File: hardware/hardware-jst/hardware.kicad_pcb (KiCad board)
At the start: 2 copper layers, 123.4 x 109.1 mm, 81 parts, among them J2 Barrel_Jack, M1 Stepper_Motor_unipolar_5pin, M10 Stepper_Motor_unipolar_5pin, M11 Stepper_Motor_unipolar_5pin, M12 Stepper_Motor_unipolar_5pin, M13 Stepper_Motor_unipolar_5pin, M14 Stepper_Motor_unipolar_5pin, M2 Stepper_Motor_unipolar_5pin, M3 Stepper_Motor_unipolar_5pin, M4 Stepper_Motor_unipolar_5pin, M5 Stepper_Motor_unipolar_5pin, M6 Stepper_Motor_unipolar_5pin, M7 Stepper_Motor_unipolar_5pin, M8 Stepper_Motor_unipolar_5pin, M9 Stepper_Motor_unipolar_5pin, SW1 SW_Push_SPDT, SW10 SW_Push_SPDT, SW11 SW_Push_SPDT, SW12 SW_Push_SPDT, SW13 SW_Push_SPDT, SW14 SW_Push_SPDT, SW15 SW_Push_SPDT, SW16 SW_Push_SPDT, SW2 SW_Push_SPDT, SW3 SW_Push_SPDT, SW4 SW_Push_SPDT, SW5 SW_Push_SPDT, SW6 SW_Push_SPDT, SW7 SW_Push_SPDT, SW8 SW_Push_SPDT, SW9 SW_Push_SPDT, U1 WeMos_D1_mini, U10 ULN2003A, U11 ULN2003A, U12 ULN2003A, U13 ULN2003A, U14 ULN2003A, U15 ULN2003A, U16 ULN2003A, U17 ULN2003A, U2 CD4051B, U3 CD4051B, U4 ULN2003A, U5 ULN2003A, U6 ULN2003A, U7 ULN2003A, U8 ULN2003A, U9 ULN2003A

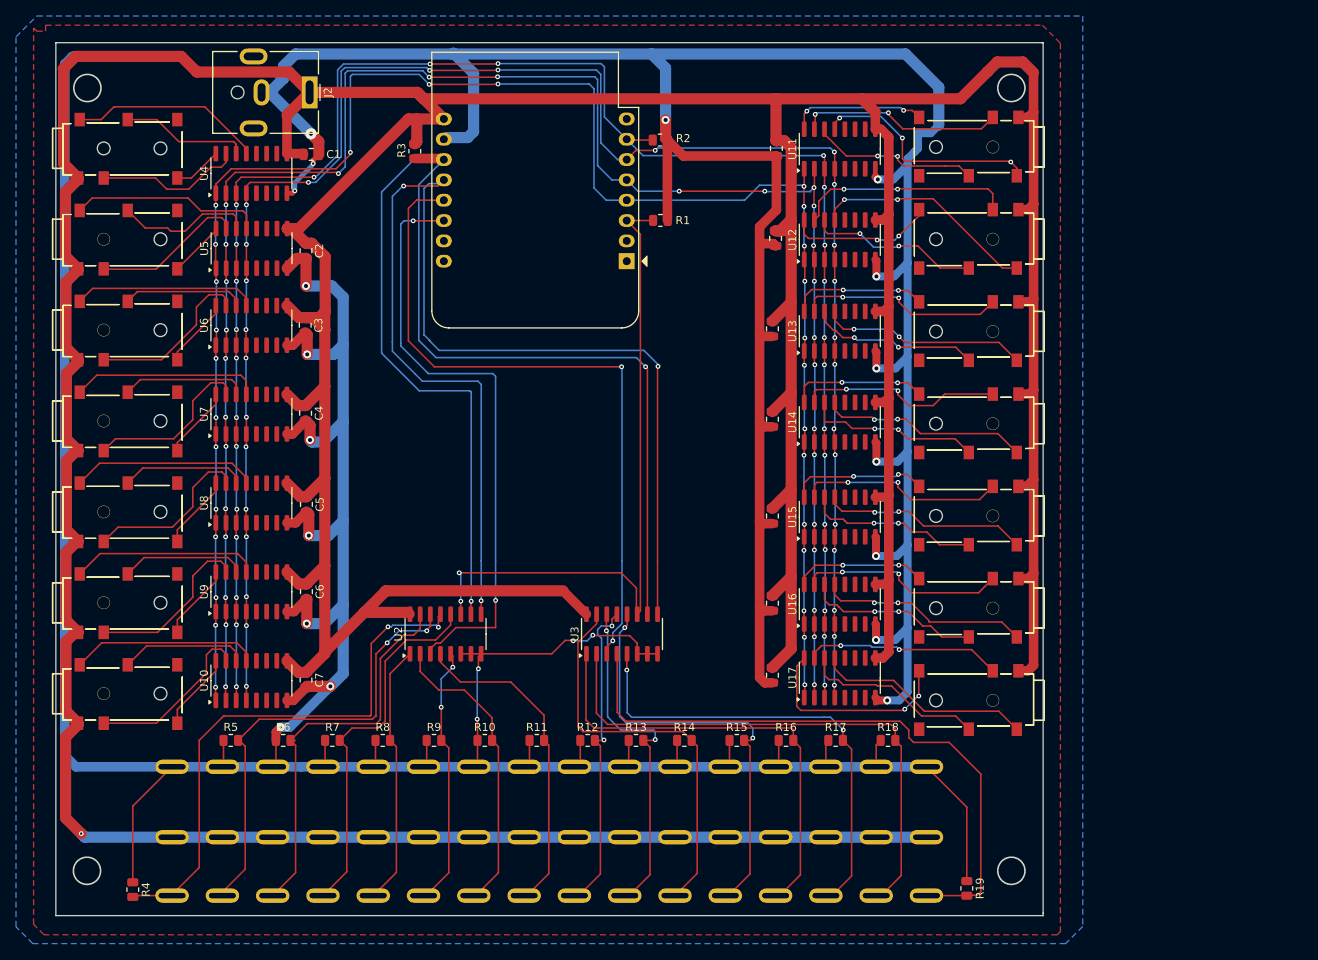
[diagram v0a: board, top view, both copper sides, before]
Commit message: partial jst conversion of pcb
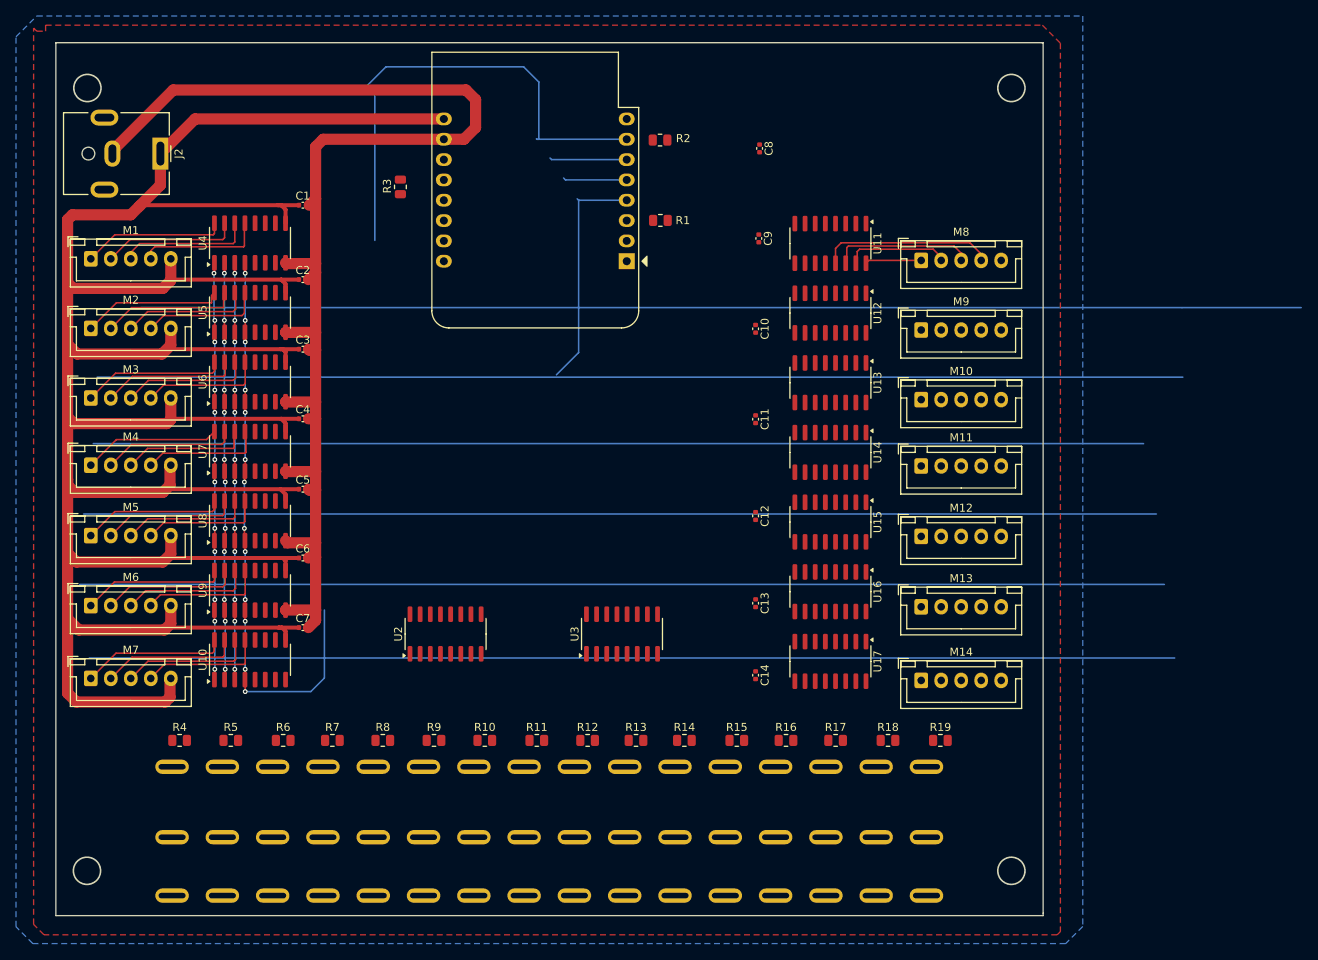
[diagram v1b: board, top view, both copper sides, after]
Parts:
- C1, C10, C11, C12, C13, C14, C2, C3, C4, C5, C6, C7, C8, C9: footprint Capacitor_SMD:C_0805_2012Metric -> Capacitor_SMD:C_0402_1005Metric
- M1, M10, M11, M12, M13, M14, M2, M3, M4, M5, M6, M7, M8, M9: footprint Connector_Audio:HOOYA-PJ-3505A_C19190915-Jack_3.5mm_PJ31060-I_Horizontal -> Connector_JST:JST_XH_B5B-XH-A_1x05_P2.50mm_Vertical
- moved J2 20.2 mm to (171.0, 57.4)
- moved R4 19.5 mm to (173.4, 130.7), turned to 0 degrees
- moved R19 18.8 mm to (268.5, 130.7), turned to 0 degrees
- moved M1 15.0 mm to (162.3, 70.5), turned to 0 degrees
- moved M8 15.0 mm to (266.1, 70.7), turned to 0 degrees
- moved M2 12.6 mm to (162.3, 79.2), turned to 0 degrees
- moved M9 12.3 mm to (266.1, 79.4), turned to 0 degrees
- moved U11 11.9 mm to (254.8, 68.6), turned to -90 degrees
- moved M3 10.4 mm to (162.3, 87.9), turned to 0 degrees
- moved M10 9.70 mm to (266.1, 88.1), turned to 0 degrees
- moved U12 9.23 mm to (254.8, 77.3), turned to -90 degrees
- moved U4 8.70 mm to (182.2, 68.5)
- moved M4 8.26 mm to (162.3, 96.3), turned to 0 degrees
- moved U5 8.01 mm to (182.2, 77.2)
- moved U6 7.07 mm to (182.2, 85.9)
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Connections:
- M1 pad 1: RED -> BLUE1
- M1 pad 2: ORANGE1 -> PINK1
- M1 pad 3: PINK1 -> YELLOW1
- M1 pad 4: YELLOW1 -> ORANGE1
- M1 pad 5: BLUE1 -> RED
- M10 pad 1: RED -> BLUE10
- M10 pad 2: ORANGE10 -> PINK10
- M10 pad 3: PINK10 -> YELLOW10
- M10 pad 4: YELLOW10 -> ORANGE10
- M10 pad 5: BLUE10 -> RED
- M11 pad 1: RED -> BLUE11
- M11 pad 2: ORANGE11 -> PINK11
- M11 pad 3: PINK11 -> YELLOW11
- M11 pad 4: YELLOW11 -> ORANGE11
- M11 pad 5: BLUE11 -> RED
- M12 pad 1: RED -> BLUE12
- M12 pad 2: ORANGE12 -> PINK12
- M12 pad 3: PINK12 -> YELLOW12
- M12 pad 4: YELLOW12 -> ORANGE12
- M12 pad 5: BLUE12 -> RED
- M13 pad 1: RED -> BLUE13
- M13 pad 2: ORANGE13 -> PINK13
- M13 pad 3: PINK13 -> YELLOW13
- M13 pad 4: YELLOW13 -> ORANGE13
- M13 pad 5: BLUE13 -> RED
- M14 pad 1: RED -> BLUE14
- M14 pad 2: ORANGE14 -> PINK14
- M14 pad 3: PINK14 -> YELLOW14
- M14 pad 4: YELLOW14 -> ORANGE14
- M14 pad 5: BLUE14 -> RED
- M2 pad 1: RED -> BLUE2
- M2 pad 2: ORANGE2 -> PINK2
- M2 pad 3: PINK2 -> YELLOW2
- M2 pad 4: YELLOW2 -> ORANGE2
- M2 pad 5: BLUE2 -> RED
- M3 pad 1: RED -> BLUE3
- M3 pad 2: ORANGE3 -> PINK3
- M3 pad 3: PINK3 -> YELLOW3
- M3 pad 4: YELLOW3 -> ORANGE3
- M3 pad 5: BLUE3 -> RED
- M4 pad 1: RED -> BLUE4
- M4 pad 2: ORANGE4 -> PINK4
- M4 pad 3: PINK4 -> YELLOW4
- M4 pad 4: YELLOW4 -> ORANGE4
- M4 pad 5: BLUE4 -> RED
- M5 pad 1: RED -> BLUE5
- M5 pad 2: ORANGE5 -> PINK5
- M5 pad 3: PINK5 -> YELLOW5
- M5 pad 4: YELLOW5 -> ORANGE5
- M5 pad 5: BLUE5 -> RED
- M6 pad 1: RED -> BLUE6
- M6 pad 2: ORANGE6 -> PINK6
- M6 pad 3: PINK6 -> YELLOW6
- M6 pad 4: YELLOW6 -> ORANGE6
- M6 pad 5: BLUE6 -> RED
- M7 pad 1: RED -> BLUE7
- M7 pad 2: ORANGE7 -> PINK7
- M7 pad 3: PINK7 -> YELLOW7
- M7 pad 4: YELLOW7 -> ORANGE7
- M7 pad 5: BLUE7 -> RED
- M8 pad 1: RED -> BLUE8
- M8 pad 2: ORANGE8 -> PINK8
- M8 pad 3: PINK8 -> YELLOW8
- M8 pad 4: YELLOW8 -> ORANGE8
- M8 pad 5: BLUE8 -> RED
- M9 pad 1: RED -> BLUE9
- M9 pad 2: ORANGE9 -> PINK9
- M9 pad 3: PINK9 -> YELLOW9
- M9 pad 4: YELLOW9 -> ORANGE9
- M9 pad 5: BLUE9 -> RED
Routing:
- net GND: track 822.2 -> 163.8 mm, vias 22 -> 0
- net RED: track 778.0 -> 360.9 mm, vias 1 -> 0
- net IN2: track 230.3 -> 60.3 mm, vias 30 -> 12
- net B: track 158.9 -> 0.00 mm, vias 2 -> 0
- net C: track 151.6 -> 0.00 mm, vias 3 -> 0
- net IN1: track 232.0 -> 81.6 mm, vias 28 -> 12
- net IN4: track 229.4 -> 82.6 mm, vias 29 -> 13
- net IN3: track 230.5 -> 113.6 mm, vias 28 -> 12
- net MUX2COM: track 86.2 -> 0.00 mm, vias 2 -> 0
- net A: track 84.9 -> 0.00 mm, vias 2 -> 0
- net SW16: track 78.2 -> 0.00 mm
- net MUX1COM: track 75.5 -> 0.00 mm, vias 2 -> 0
- net SW1: track 68.7 -> 0.00 mm, vias 2 -> 0
- net SW15: track 68.4 -> 0.00 mm
- net SW14: track 58.2 -> 0.00 mm, vias 2 -> 0
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
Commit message: half way done
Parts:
- moved C8 11.4 mm to (248.4, 67.8), turned to 90 degrees
- moved C9 6.94 mm to (248.1, 74.5)
- moved C10 4.87 mm to (245.4, 84.1)
- moved C11 4.87 mm to (245.4, 95.4)
- moved C13 4.87 mm to (245.4, 118.4)
- moved C12 4.87 mm to (245.4, 107.5)
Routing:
- net RED: track 360.9 -> 813.3 mm
- net GND: track 163.8 -> 225.9 mm
- net IN1: track 81.6 -> 103.6 mm, vias 12 -> 15
- net ORANGE9: track 0.00 -> 21.4 mm
- net YELLOW9: track 0.00 -> 16.7 mm
- net PINK9: track 0.00 -> 12.5 mm
- net BLUE9: track 0.00 -> 7.05 mm

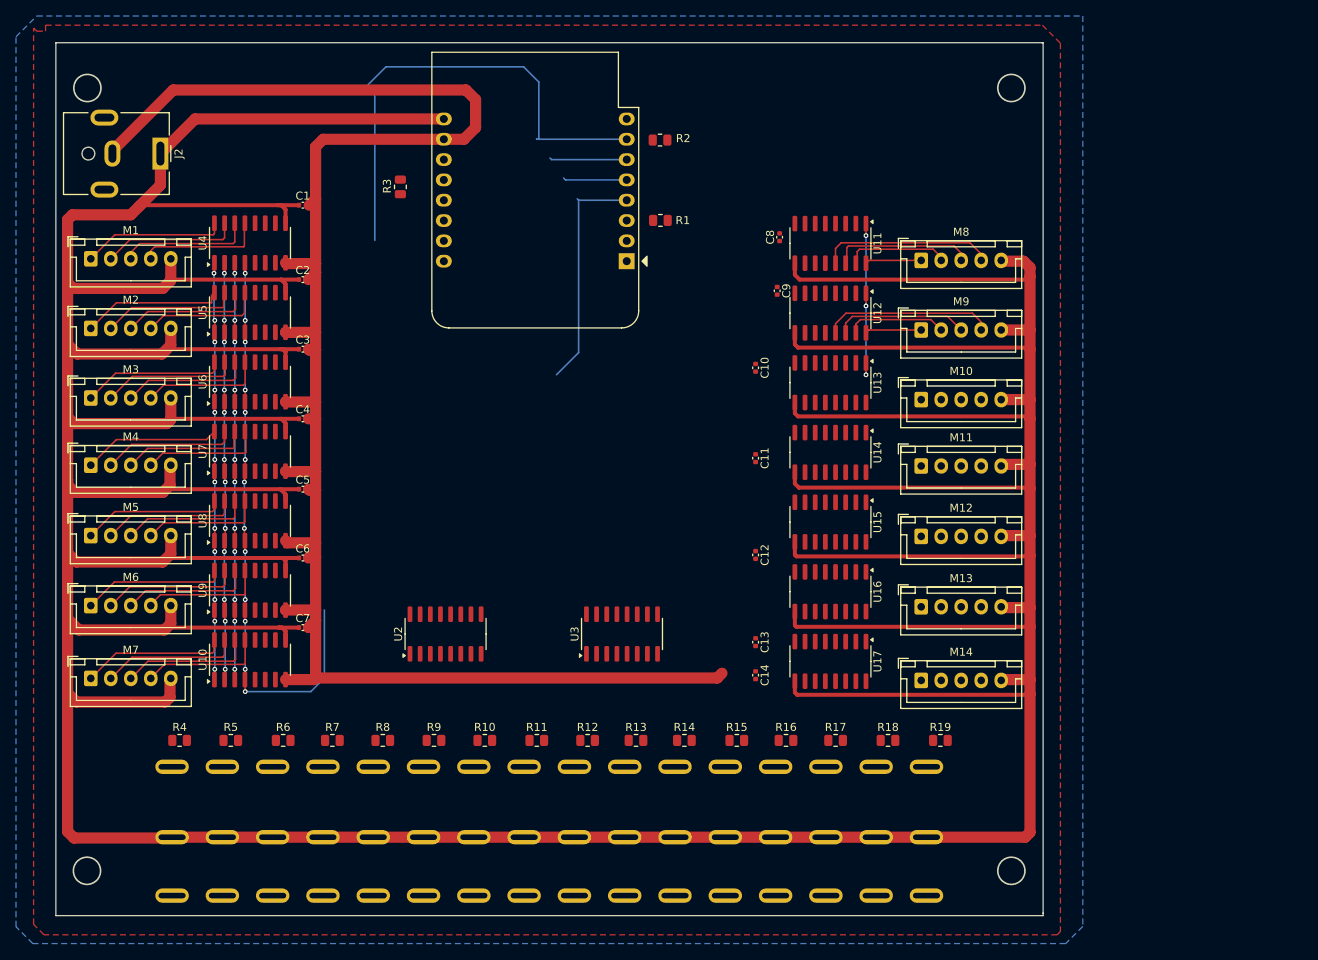
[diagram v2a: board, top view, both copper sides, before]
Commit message: finalised JST switch version of the pcb
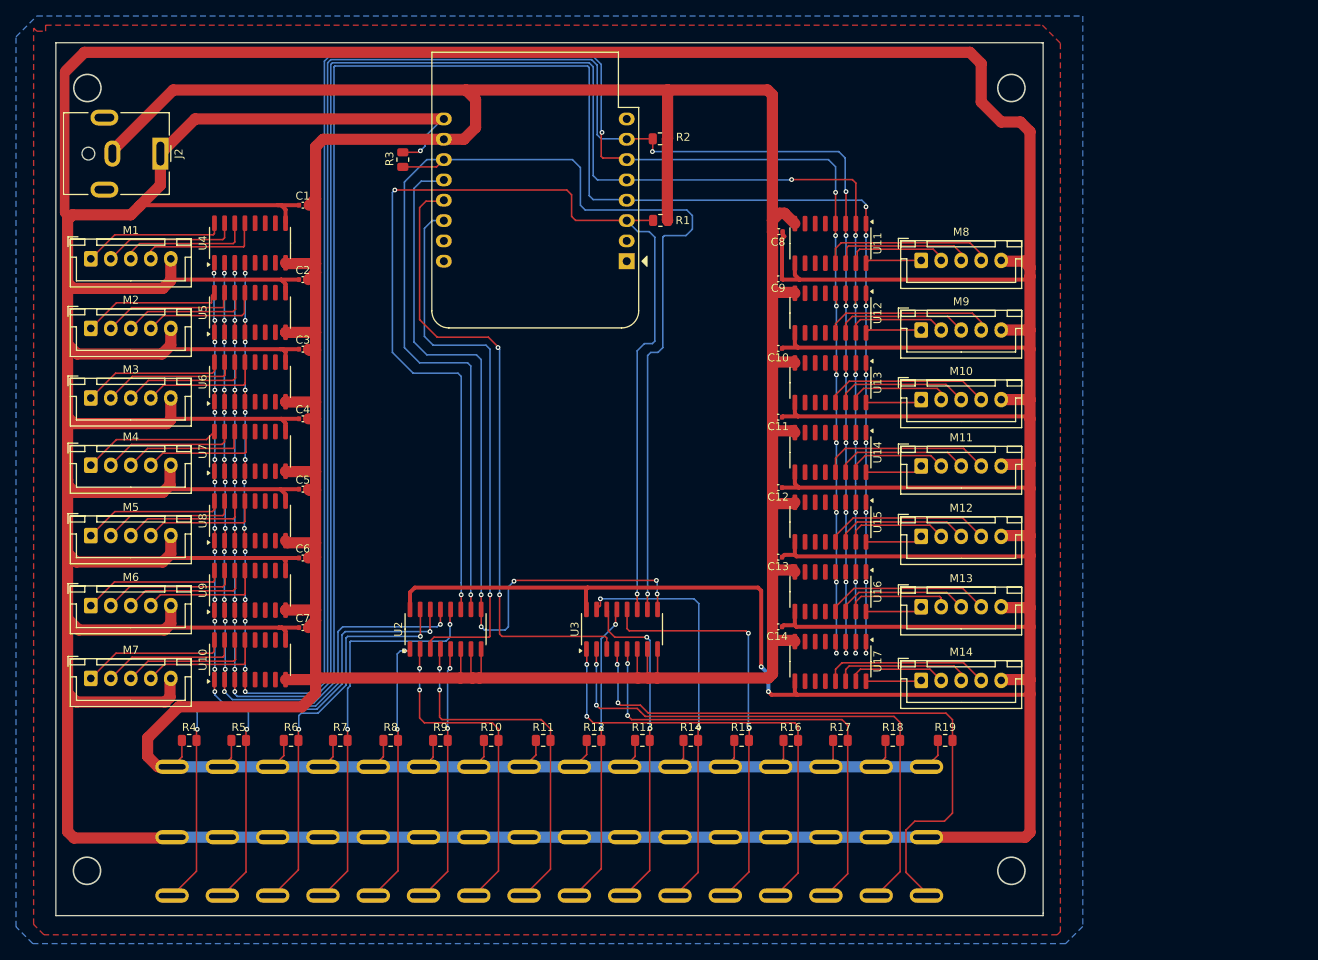
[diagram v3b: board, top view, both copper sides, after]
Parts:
- moved C13 11.0 mm to (248.2, 107.8), turned to 180 degrees
- moved C12 8.88 mm to (248.2, 99.1), turned to 180 degrees
- moved C14 6.67 mm to (248.2, 116.5), turned to 180 degrees
- moved C11 5.85 mm to (248.2, 90.3), turned to 180 degrees
- moved C10 3.72 mm to (248.2, 81.7), turned to 180 degrees
- moved R3 3.43 mm to (201.3, 58.1)
- moved C9 1.50 mm to (248.2, 73.0), turned to 180 degrees
- moved R4 1.20 mm to (174.6, 130.7)
- moved R6 0.99 mm to (187.3, 130.7)
- moved R7 0.99 mm to (193.5, 130.7)
- moved R5 0.99 mm to (180.8, 130.7)
- moved R8 0.99 mm to (199.8, 130.7)
- moved R13 0.80 mm to (231.2, 130.7)
- moved R14 0.80 mm to (237.3, 130.7)
- moved R9 0.80 mm to (206.0, 130.7)
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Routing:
- net GND: track 225.9 -> 588.9 mm
- net RED: track 813.3 -> 1068.8 mm, vias 0 -> 3
- net IN2: track 60.3 -> 292.7 mm, vias 12 -> 21
- net IN4: track 82.6 -> 287.8 mm, vias 13 -> 22
- net IN1: track 103.6 -> 295.1 mm, vias 15 -> 21
- net IN3: track 113.6 -> 290.1 mm, vias 12 -> 22
- net B: track 0.00 -> 162.9 mm, vias 0 -> 2
- net A: track 0.00 -> 147.3 mm, vias 0 -> 3
- net C: track 0.00 -> 97.3 mm, vias 0 -> 5
- net MUX2COM: track 0.00 -> 79.6 mm, vias 0 -> 2
- net SW16: track 0.00 -> 77.1 mm, vias 0 -> 2
- net MUX1COM: track 0.00 -> 69.8 mm, vias 0 -> 1
- net SW15: track 0.00 -> 68.8 mm, vias 0 -> 2
- net SW1: track 0.00 -> 64.8 mm, vias 0 -> 2
- net SW14: track 0.00 -> 58.8 mm, vias 0 -> 2
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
